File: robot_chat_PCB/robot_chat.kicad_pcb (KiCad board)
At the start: 4 copper layers, 90 x 72.1 mm, 108 parts, among them IC401 NCS199A3RSQT2G, IC402 NCS199A3RSQT2G, J201 Conn_02x07_Odd_Even, J301 Conn_01x02, J401 Conn_01x06, J402 Conn_01x06, J501 Conn_01x03, J502 Conn_01x08, J503 Conn_01x03, J504 Conn_01x02, J601 Conn_01x06, SW201 SW_Push, SW301 SW_SPDT_MSM, SW601 SW_Push, SW602 SW_Push, U201 STM32G070RBTx, U301 MP1475DJ-LF-P, U302 MIC5317-3.3xM5, U401 ZXBM5210-SP-13, U402 ZXBM5210-SP-13, U501 LSM6DSM, Y201 16MHz

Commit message: Mise à jour placement
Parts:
- +3V301: value TestPoint -> 3.3V
- +5V301: value TestPoint -> 5V
- C302, C303, C305, C501, C502: footprint Capacitor_SMD:C_0603_1608Metric -> Capacitor_SMD:C_0402_1005Metric
- CS201: value TestPoint -> CS
- D301: value LED_Small -> 5V
- D304: value LED_Small -> 3.3V
- D501: value LED_Small -> Bump
- D601: value LED_Small -> Border_Detect
- D602: value LED_Small -> Status
- D603: value LED_Small -> Error
- D604: value LED_Small -> Debug_1
- D605: value LED_Small -> Debug_2
- J201: value Conn_02x07_Odd_Even -> STLink
- J301: value Conn_01x02 -> Bat
- J401: value Conn_01x06 -> L_Mot
- J402: value Conn_01x06 -> R_Mot
- J501: value Conn_01x03 -> F_Detect
- J502: value Conn_01x08 -> Lidar
- J503: value Conn_01x03 -> B_Detect
- J504: value Conn_01x02 -> Bump
- J601: value Conn_01x06 -> BT; footprint Connector_JST:JST_XH_S6B-XH-A_1x06_P2.50mm_Horizontal -> Connector_PinSocket_2.54mm:PinSocket_1x06_P2.54mm_Horizontal
- LIDAR_RX201: value TestPoint -> L-RX
- LIDAR_TX201: value TestPoint -> L-TX
- SDI201: value TestPoint -> MOSI
- SDO201: value TestPoint -> MISO
- SPI_CLK201: value TestPoint -> SPI_CLK
- SW201: value SW_Push -> RST
- SW601: value SW_Push -> Status
- SW602: value SW_Push -> Start
- U401, U402: value ZXBM5210-SP-13 -> ZXBM5210-SP
- moved D601 55.7 mm to (87.0, 98.5), turned to -90 degrees
- moved D602 54.1 mm to (81.0, 98.5), turned to -90 degrees
- moved D605 53.6 mm to (63.0, 98.5), turned to -90 degrees
- moved D603 53.2 mm to (75.0, 98.5), turned to -90 degrees
- moved D604 52.8 mm to (69.0, 98.5), turned to -90 degrees
- moved D203 52.1 mm to (92.5, 151.2)
- moved D204 51.9 mm to (89.2, 151.2)
- moved D205 51.9 mm to (87.2, 151.2)
- moved D201 51.8 mm to (93.5, 141.2)
- moved D202 51.8 mm to (94.5, 151.2)
- moved J201 51.8 mm to (91.5, 146.2)
- moved D206 51.8 mm to (88.4, 141.2)
- moved R602 49.4 mm to (87.0, 103.0), turned to -90 degrees
- moved R606 48.1 mm to (63.0, 103.0), turned to -90 degrees
- moved R603 47.8 mm to (81.0, 103.0), turned to -90 degrees
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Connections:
- D304 pad 1: Net-(D304-K) -> GND
- D304 pad 2: +3.3V -> Net-(D304-A)
- D501 pad 1: Net-(D501-K) -> GND
- D501 pad 2: /STM/BUMPER_SW -> Net-(D501-A)
- J401 pad 1: /Motor drivers/MOTOR_L- -> /Motor drivers/MOTOR_L+
- J401 pad 6: /Motor drivers/MOTOR_L+ -> /Motor drivers/MOTOR_L-
- J402 pad 1: /Motor drivers/MOTOR_R- -> /Motor drivers/MOTOR_R+
- J402 pad 6: /Motor drivers/MOTOR_R+ -> /Motor drivers/MOTOR_R-
- R309 pad 1: GND -> Net-(D304-A)
- R309 pad 2: Net-(D304-K) -> +3.3V
- R501 pad 1: GND -> Net-(D501-A)
- R501 pad 2: Net-(D501-K) -> /STM/BUMPER_SW
- U401 pad 1: /Motor drivers/MOTOR_L- -> /Motor drivers/MOTOR_R-
- U401 pad 2: /Motor drivers/RSENSE_L- -> /Motor drivers/RSENSE_R-
- U401 pad 4: /Motor drivers/FWD_L -> /Motor drivers/FWD_R
- U401 pad 5: /Motor drivers/REV_L -> /Motor drivers/REV_R
- U401 pad 7: /Motor drivers/MOTOR_L+ -> /Motor drivers/MOTOR_R+
- U401 pad 9: (no net) -> GND
- U402 pad 1: /Motor drivers/MOTOR_R- -> /Motor drivers/MOTOR_L-
- U402 pad 2: /Motor drivers/RSENSE_R- -> /Motor drivers/RSENSE_L-
- U402 pad 4: /Motor drivers/FWD_R -> /Motor drivers/FWD_L
- U402 pad 5: /Motor drivers/REV_R -> /Motor drivers/REV_L
- U402 pad 7: /Motor drivers/MOTOR_R+ -> /Motor drivers/MOTOR_L+
- U402 pad 9: (no net) -> GND
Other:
- board size 90 x 72.1 mm -> 90 x 72 mm
- board text removed: "D0"
- board text removed: "D1"
- board text removed: "D2"
- board text removed: "D3"
- board text removed: "D4"

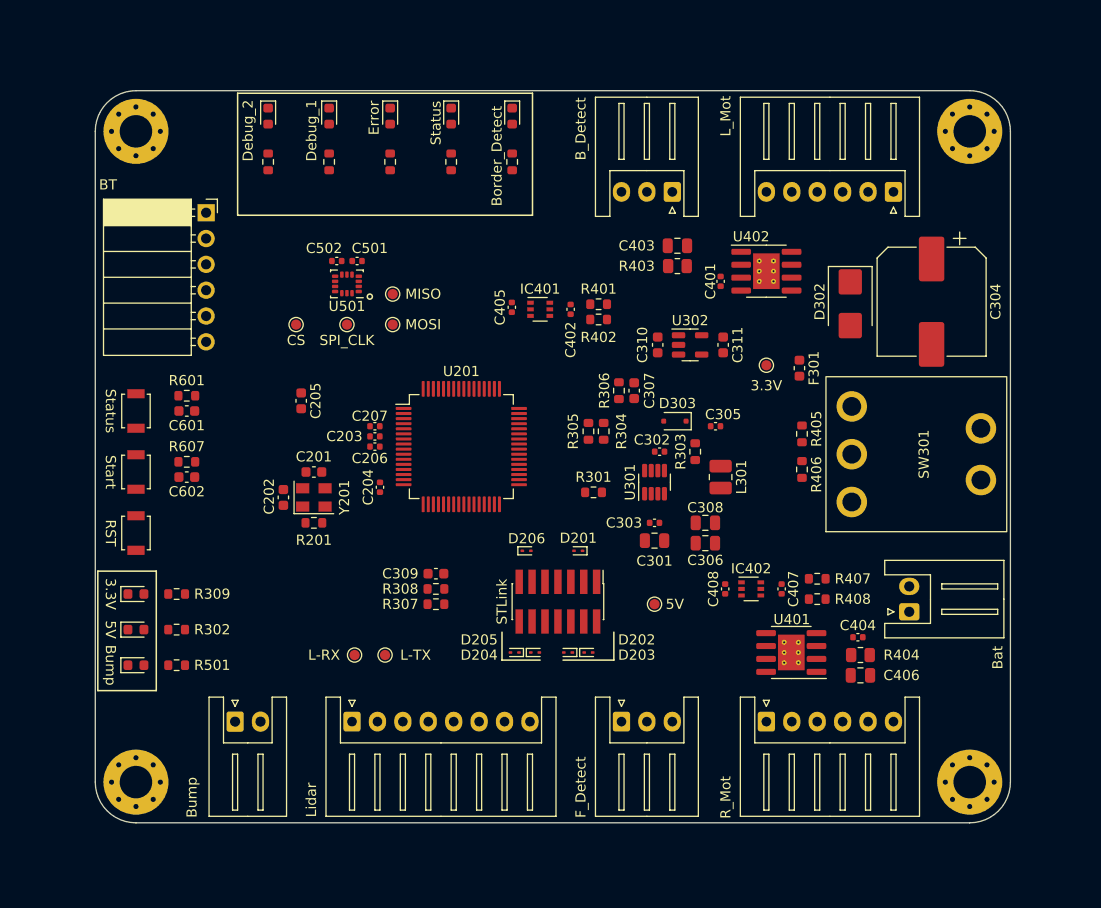
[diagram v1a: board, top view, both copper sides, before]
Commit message: changed Rsense position
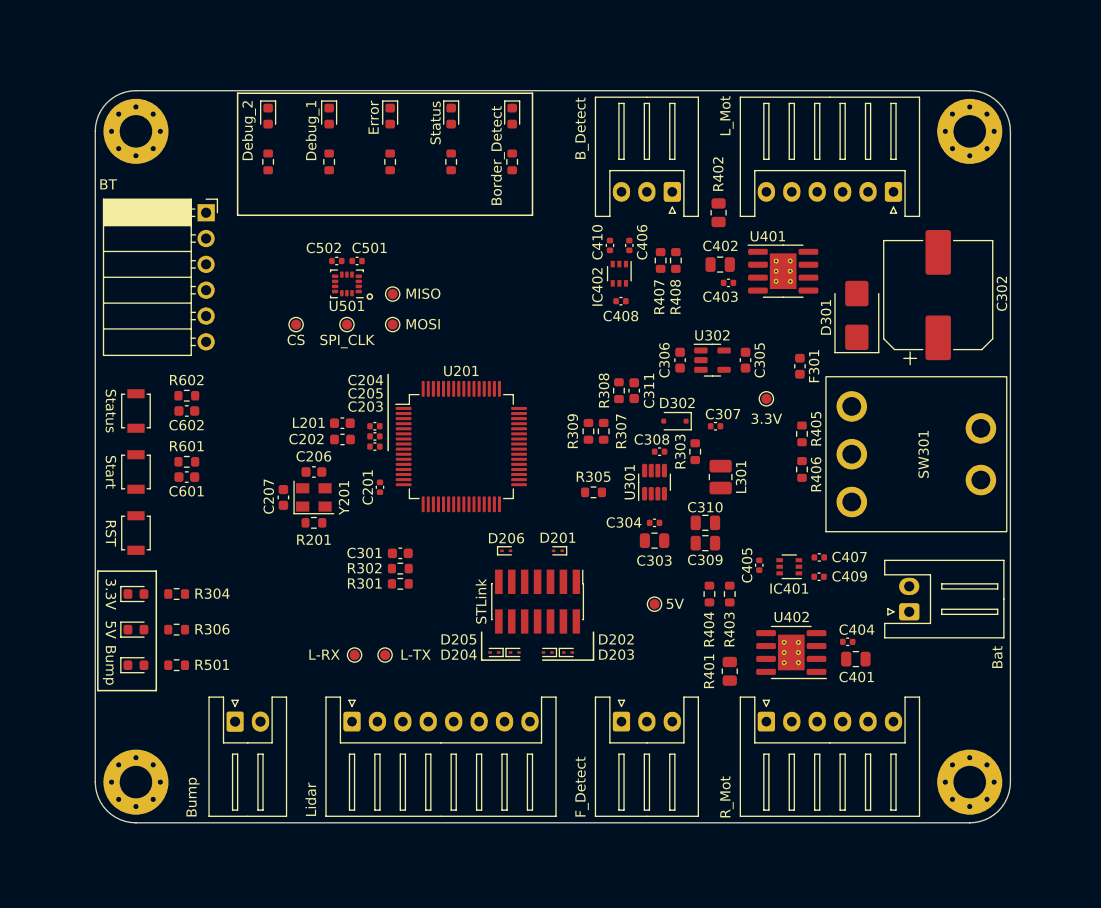
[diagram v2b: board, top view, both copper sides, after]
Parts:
- added C406: 0.1uF, Capacitor_SMD:C_0402_1005Metric, F.Cu at (98.5, 111.2)
- added C409: 0.1uF, Capacitor_SMD:C_0402_1005Metric, F.Cu at (117.2, 143.8)
- added L201: 2.2u, Inductor_SMD:L_0603_1608Metric, F.Cu at (70.3, 130.3)
- moved R401 12.9 mm to (108.4, 153.1), turned to 90 degrees
- moved C410 11.4 mm to (96.6, 111.2)
- moved R404 10.6 mm to (106.4, 145.5), turned to 90 degrees
- moved C407 9.76 mm to (117.2, 141.9), turned to 0 degrees
- moved R408 9.56 mm to (103.1, 112.7), turned to -90 degrees
- moved R403 8.73 mm to (108.4, 145.5), turned to 90 degrees
- moved IC402 8.54 mm to (97.5, 114.0), turned to -90 degrees
- moved R407 7.46 mm to (101.6, 112.7), turned to -90 degrees
- moved R402 6.63 mm to (107.3, 108.0), turned to -90 degrees
- moved C408 5.01 mm to (97.7, 116.7), turned to 180 degrees
- moved C202 4.61 mm to (70.3, 128.7), turned to 0 degrees
- moved C402 4.59 mm to (107.5, 113.1), turned to 180 degrees
- moved IC401 4.34 mm to (114.2, 142.8), turned to 180 degrees
- moved C301 4.03 mm to (76.0, 141.5)
- moved R301 4.03 mm to (76.0, 144.5)
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- renumbered C204 to C201, C205 to C202, C206 to C203, C207 to C204, C203 to C205, C201 to C206, C202 to C207, C309 to C301, C304 to C302, C301 to C303, C303 to C304, C311 to C305, C310 to C306, C305 to C307, C302 to C308, C306 to C309, C308 to C310, C307 to C311, C406 to C401, C403 to C402, C401 to C403, C407 to C405, C408 to C407, C402 to C408, C405 to C410, C602 to C601, C601 to C602, D302 to D301, D303 to D302, D304 to D303, D301 to D304, IC402 to IC401, IC401 to IC402, J504 to J501, J501 to J504, R307 to R301, R308 to R302, R309 to R304, R301 to R305, R302 to R306, R304 to R307, R306 to R308, R305 to R309, R404 to R401, R403 to R402, R407 to R403, R408 to R404, R401 to R407, R402 to R408, R607 to R601, R601 to R602, R602 to R603, R603 to R604, R604 to R605, R605 to R606, R606 to R607, SW602 to SW601, SW601 to SW602, U402 to U401, U401 to U402
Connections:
- C205 pad 2: +3.3V -> Net-(U201-VREF+)
- J401 pad 6: /Motor drivers/MOTOR_L- -> /Motor drivers/RSENSE_L-
- J402 pad 1: /Motor drivers/MOTOR_R+ -> /Motor drivers/RSENSE_R-
- R401 pad 1: +7.5V -> /Motor drivers/RSENSE_R-
- R401 pad 2: /Motor drivers/RSENSE_R- -> /Motor drivers/MOTOR_R+
- R402 pad 1: +7.5V -> /Motor drivers/RSENSE_L-
- R402 pad 2: /Motor drivers/RSENSE_L- -> /Motor drivers/MOTOR_L-
- R403 pad 1: +7.5V -> /Motor drivers/MOTOR_R+
- R407 pad 1: +7.5V -> /Motor drivers/MOTOR_L-
- U201 pad 7: +3.3V -> Net-(U201-VREF+)
- U401 pad 2: /Motor drivers/RSENSE_L- -> +7.5V
- U402 pad 2: /Motor drivers/RSENSE_R- -> +7.5V

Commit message: Mise à jour led bumper
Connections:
- J501 pad 1: /STM/BUMPER_SW -> +3.3V
- J501 pad 2: GND -> /STM/BUMPER_SW
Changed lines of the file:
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@@
       (stroke (width 0.1) (type solid)) (layer "F.Fab"))
     (pad "1" thru_hole roundrect (at 0 0) (size 1.7 2) (drill 1) (layers "*.Cu" "*.Mask") (roundrect_rratio 0.147059)
-      (net 20 "/STM/BUMPER_SW") (pinfunction "Pin_1") (pintype "passive"))
+      (net 1 "+3.3V") (pinfunction "Pin_1") (pintype "passive"))
     (pad "2" thru_hole oval (at 2.5 0) (size 1.7 2) (drill 1) (layers "*.Cu" "*.Mask")
-      (net 3 "GND") (pinfunction "Pin_2") (pintype "passive"))
+      (net 20 "/STM/BUMPER_SW") (pinfunction "Pin_2") (pintype "passive"))
     (model "${KICAD6_3DMODEL_DIR}/Connector_JST.3dshapes/JST_XH_S2B-XH-A_1x02_P2.50mm_Horizontal.wrl"
       (offset (xyz 0 0 0))

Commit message: Routage
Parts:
- moved CS201 15.1 mm to (80.4, 122.7)
- moved +5V301 14.6 mm to (113.0, 138.2)
- moved SPI_CLK201 10.2 mm to (80.9, 120.3)
- moved C501 9.10 mm to (80.8, 111.8)
- moved C502 9.10 mm to (78.8, 111.8)
- moved U501 9.10 mm to (79.8, 114.0)
- moved SDO201 7.45 mm to (82.7, 116.0)
- moved SDI201 6.25 mm to (81.4, 117.9)
- moved LIDAR_TX201 4.27 mm to (78.6, 150.3)
- moved LIDAR_RX201 3.44 mm to (74.9, 152.0)
- moved R601 2.50 mm to (55.0, 135.0)
- moved C307 1.80 mm to (107.6, 130.7)
- moved C309 1.30 mm to (106.0, 139.2)
- moved C310 1.30 mm to (106.0, 137.2)
- moved D201 1.30 mm to (90.2, 141.3)
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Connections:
- C403 pad 1: +3V3 -> +3.3V
- C404 pad 1: +3V3 -> +3.3V
- R407 pad 1: /Motor drivers/MOTOR_L- -> /Motor drivers/RSENSE_L-
- R408 pad 1: /Motor drivers/RSENSE_L- -> /Motor drivers/MOTOR_L-
- U201 pad 25: /STM/LIDAR_TX -> /STM/LIDAR_RX
- U201 pad 26: /STM/LIDAR_RX -> /STM/LIDAR_TX
- U201 pad 27: /Motor drivers/I_READ_L -> unconnected-(U201-PB0-Pad27)
- U201 pad 30: unconnected-(U201-PB10-Pad30) -> /Motor drivers/I_READ_L
- U201 pad 40: /STM/IMU_SPI_CLK -> unconnected-(U201-PD8-Pad40)
- U201 pad 52: /STM/IMU_SPI_CS -> unconnected-(U201-PD2-Pad52)
- U201 pad 57: unconnected-(U201-PB3-Pad57) -> /STM/IMU_SPI_CLK
- U201 pad 58: USER_LED_0 -> /STM/IMU_SPI_CS
- U201 pad 59: USER_LED_1 -> unconnected-(U201-PB5-Pad59)
- U201 pad 60: unconnected-(U201-PB6-Pad60) -> USER_LED_0
- U201 pad 61: unconnected-(U201-PB7-Pad61) -> USER_LED_1
- U401 pad 3: +3V3 -> +3.3V
- U401 pad 6: +3V3 -> +3.3V
- U402 pad 3: +3V3 -> +3.3V
- U402 pad 6: +3V3 -> +3.3V
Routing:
- net Net-(D304-K): track 0.00 -> 135.5 mm, vias 0 -> 2
- net /STM/~{RST}: track 0.00 -> 61.7 mm, vias 0 -> 2
- net /STM/BACK_BORDER_DETECT: track 0.00 -> 58.7 mm, vias 0 -> 1
- net /Motor drivers/FWD_R: track 0.00 -> 55.2 mm, vias 0 -> 2
- net /Motor drivers/ENCODER_L_B: track 0.00 -> 55.0 mm, vias 0 -> 1
- net /Motor drivers/ENCODER_L_A: track 0.00 -> 54.0 mm, vias 0 -> 1
- net +3.3V: track 0.00 -> 50.1 mm, vias 0 -> 19
- net /Motor drivers/VREF: track 0.00 -> 49.9 mm, vias 0 -> 4
- net /STM/FRONT_BORDER_DETECT: track 0.00 -> 49.2 mm
- net /Motor drivers/ENCODER_R_B: track 0.00 -> 47.9 mm, vias 0 -> 1
- net /Motor drivers/ENCODER_R_A: track 0.00 -> 45.8 mm, vias 0 -> 1
- net /Motor drivers/REV_R: track 0.00 -> 41.8 mm, vias 0 -> 2
- net /STM/BUMPER_SW: track 0.00 -> 41.8 mm
- net /Motor drivers/FWD_L: track 0.00 -> 40.3 mm, vias 0 -> 2
- net /Motor drivers/I_READ_R: track 0.00 -> 38.1 mm
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- added copper zone on F.Cu, net +3.3V
- added copper zone on In2.Cu, net +3.3V
- added copper zone on F.Cu, net +5V
- added copper zone on In2.Cu, net +5V
- added copper zone on F.Cu, net +7.5V
- added copper zone on In2.Cu, net +7.5V
- added copper zone on B.Cu, net GND
- added copper zone on F.Cu, net GND
- added copper zone on In1.Cu, net GND
- added copper zone on F.Cu, net Net-(F301-Pad2)
- added copper zone on F.Cu, net Net-(J301-Pin_1)
- added copper zone on B.Cu, net Net-(U301-SW)
- added copper zone on F.Cu, net Net-(U301-SW)

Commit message: Routage final v1
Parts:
- added G***: LOGO, LOGO, F.Cu at (67.3, 116.8)
- moved SDO201 0.41 mm to (82.8, 116.4)
- moved C404 0.10 mm to (119.4, 150.2)
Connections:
- SW301 pad 4: (no net) -> GND
- SW301 pad 5: (no net) -> GND
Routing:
- net Net-(U201-VREF+): track 6.34 -> 10.8 mm
- net +7.5V: track 33.2 -> 34.2 mm
- net GND: vias 18 -> 283

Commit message: routage final v1.1
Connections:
- U201 pad 37: unconnected-(U201-PA9/NC-Pad37) -> /Motor drivers/ENCODER_L_A
- U201 pad 43: /Motor drivers/ENCODER_L_A -> unconnected-(U201-PA11/PA9-Pad43)
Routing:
- net /Motor drivers/ENCODER_L_A: track 53.5 -> 56.5 mm
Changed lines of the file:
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@@
   (net 93 "unconnected-(U201-PB2-Pad29)")
   (net 94 "unconnected-(U201-PB13-Pad33)")
-  (net 95 "unconnected-(U201-PA9{slash}NC-Pad37)")
+  (net 95 "unconnected-(U201-PA11{slash}PA9-Pad43)")
   (net 96 "unconnected-(U201-PD9-Pad41)")
   (net 97 "unconnected-(U201-PA10{slash}NC-Pad42)")
@@
       (net 26 "/Motor drivers/ENCODER_L_B") (pinfunction "PA8") (pintype "bidirectional"))
     (pad "37" smd roundrect (at 5.675 1.75) (size 1.55 0.3) (layers "F.Cu" "F.Paste" "F.Mask") (roundrect_rratio 0.25)
-      (net 95 "unconnected-(U201-PA9{slash}NC-Pad37)") (pinfunction "PA9/NC") (pintype "bidirectional+no_connect"))
+      (net 25 "/Motor drivers/ENCODER_L_A") (pinfunction "PA9/NC") (pintype "bidirectional"))
     (pad "38" smd roundrect (at 5.675 1.25) (size 1.55 0.3) (layers "F.Cu" "F.Paste" "F.Mask") (roundrect_rratio 0.25)
       (net 37 "/STM/LIDAR_EN") (pinfunction "PC6") (pintype "bidirectional"))
@@
       (net 97 "unconnected-(U201-PA10{slash}NC-Pad42)") (pinfunction "PA10/NC") (pintype "bidirectional+no_connect"))
     (pad "43" smd roundrect (at 5.675 -1.25) (size 1.55 0.3) (layers "F.Cu" "F.Paste" "F.Mask") (roundrect_rratio 0.25)
-      (net 25 "/Motor drivers/ENCODER_L_A") (pinfunction "PA11/PA9") (pintype "bidirectional"))
+      (net 95 "unconnected-(U201-PA11{slash}PA9-Pad43)") (pinfunction "PA11/PA9") (pintype "bidirectional+no_connect"))
     (pad "44" smd roundrect (at 5.675 -1.75) (size 1.55 0.3) (layers "F.Cu" "F.Paste" "F.Mask") (roundrect_rratio 0.25)
       (net 98 "unconnected-(U201-PA12{slash}PA10-Pad44)") (pinfunction "PA12/PA10") (pintype "bidirectional+no_connect"))
@@
   (segment (start 103.8 111.223896) (end 106.111396 108.9125) (width 0.25) (layer "F.Cu") (net 24))
   (segment (start 108.2425 108.9125) (end 111.175 111.845) (width 1) (layer "F.Cu") (net 24))
-  (segment (start 89.05 129.75) (end 87.675 129.75) (width 0.25) (layer "F.Cu") (net 25))
-  (segment (start 89.8 109.8) (end 89.8 129) (width 0.25) (layer "F.Cu") (net 25))
-  (segment (start 89.8 129) (end 89.05 129.75) (width 0.25) (layer "F.Cu") (net 25))
-  (segment (start 89.5 109.5) (end 89.8 109.8) (width 0.25) (layer "F.Cu") (net 25))
+  (segment (start 89.8 109.8) (end 89.5 109.5) (width 0.25) (layer "F.Cu") (net 25))
+  (segment (start 89.8 132) (end 89.8 109.8) (width 0.25) (layer "F.Cu") (net 25))
+  (segment (start 89.05 132.75) (end 89.8 132) (width 0.25) (layer "F.Cu") (net 25))
+  (segment (start 87.675 132.75) (end 89.05 132.75) (width 0.25) (layer "F.Cu") (net 25))
   (via (at 89.5 109.5) (size 0.5) (drill 0.3) (layers "F.Cu" "B.Cu") (net 25))
   (segment (start 115.95 109.5) (end 119.5 105.95) (width 0.25) (layer "B.Cu") (net 25))
